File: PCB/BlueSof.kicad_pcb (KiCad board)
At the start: 2 copper layers, 134.3 x 100.2 mm, 117 parts, among them J1 USB_C_Receptacle_USB2.0, J2 Conn_01x01_Female, J3 Conn_01x04_Female, J4 Conn_01x01_Female, J5 USB_C_Receptacle_USB2.0, Q1 A03407, Q2 A03407, SW1 SW_PUSH, SW10 SW_PUSH, SW11 SW_PUSH, SW12 SW_PUSH, SW13 SW_PUSH, SW14 SW_PUSH, SW15 SW_PUSH, SW16 SW_PUSH, SW17 SW_PUSH, SW18 SW_PUSH, SW19 SW_PUSH, SW2 SW_PUSH, SW20 SW_PUSH, SW21 SW_PUSH, SW22 SW_PUSH, SW23 SW_PUSH, SW24 SW_PUSH, SW25 Rotary_Encoder_Switch, SW26 SW_PUSH, SW27 SW_PUSH, SW28 SW_PUSH, SW29 SW_PUSH, SW3 SW_PUSH, SW30 SW_PUSH, SW31 SW_Push, SW32 SW_Push, SW4 SW_PUSH, SW5 SW_PUSH, SW6 SW_PUSH, SW7 SW_PUSH, SW8 SW_PUSH, SW9 SW_PUSH, U1 LN2054Y42AMR, U2 E73-2G4M08S1C, U3 AP2112K-3.3, U4 E73-2G4M08S1C, U5 LN2054Y42AMR, U6 AP2112K-3.3, Y1 32.768kHz, Y2 32.768kHz

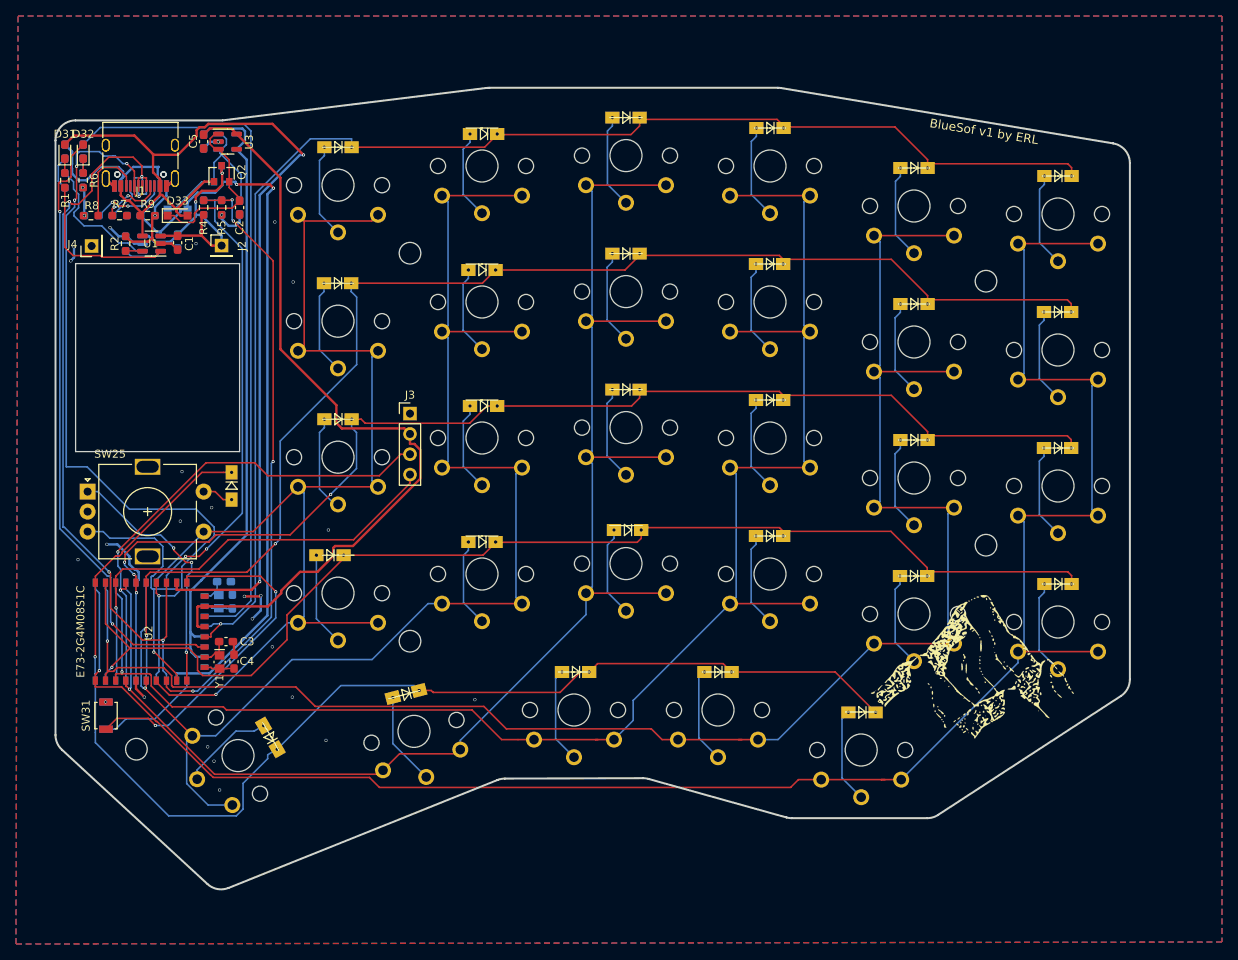
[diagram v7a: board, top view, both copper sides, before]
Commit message: R2 version with minor fixes
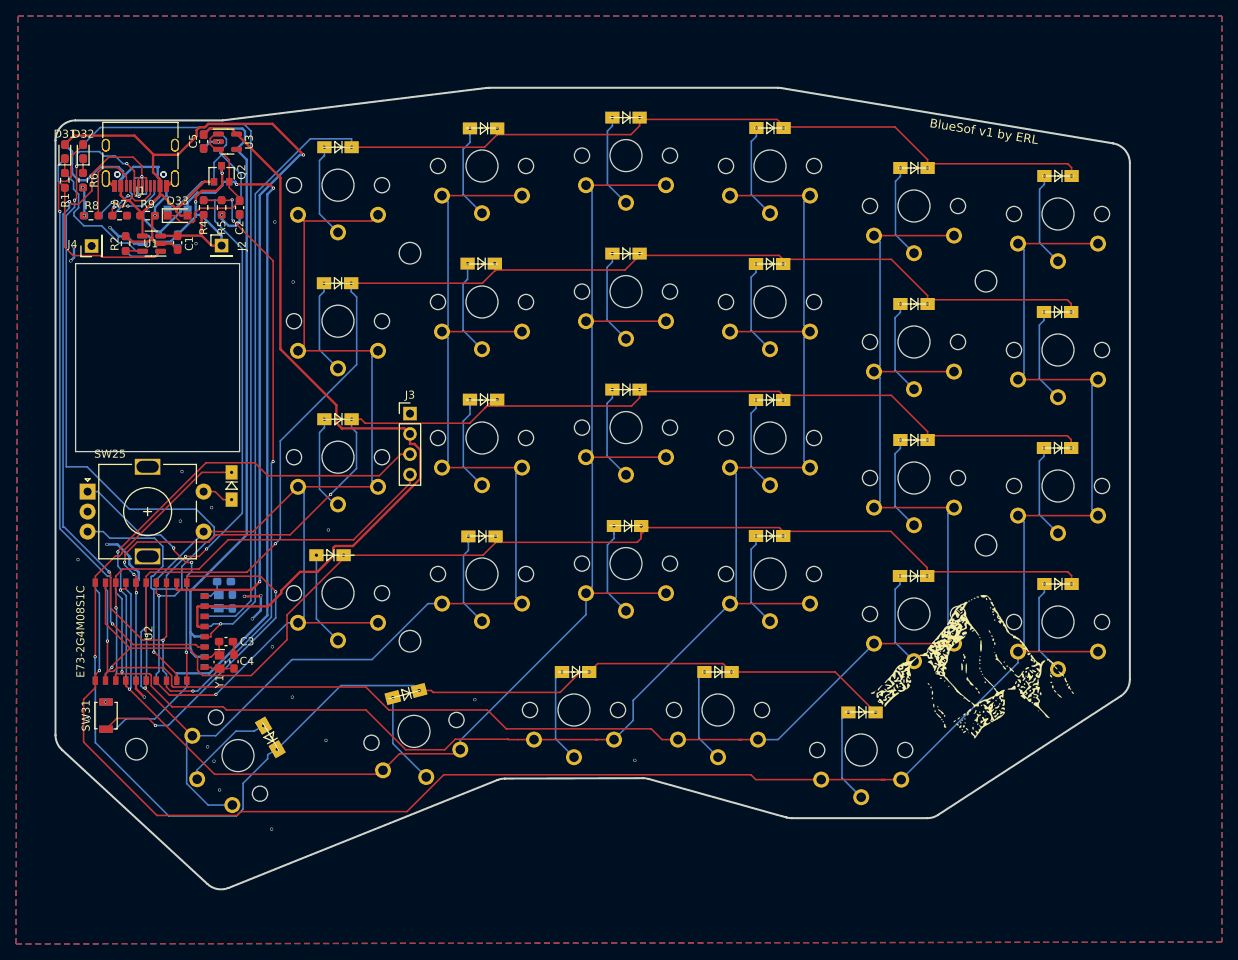
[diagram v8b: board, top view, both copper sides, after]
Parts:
- moved D8 0.81 mm to (139.4, 63.9)
- moved D14 0.80 mm to (139.7, 80.9)
- moved D2 0.70 mm to (139.7, 47.0)
- moved D20 0.70 mm to (139.5, 98.0)
- moved D21 0.50 mm to (157.7, 96.7)
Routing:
- net col0: track 235.2 -> 244.8 mm
- net row3: track 150.4 -> 152.5 mm
- net row2: track 153.7 -> 155.7 mm
- net Net-(D14-Pad2): track 11.2 -> 12.3 mm
- net col2: track 195.2 -> 196.3 mm
- net Net-(D21-Pad2): track 11.4 -> 12.4 mm
- net row1: track 164.6 -> 165.5 mm
- net Net-(D20-Pad2): track 11.1 -> 11.9 mm
- net Net-(D2-Pad2): track 11.2 -> 12.0 mm
- net row0: track 174.3 -> 175.0 mm
- net Net-(D8-Pad2): track 11.2 -> 11.9 mm
- net GND: vias 29 -> 32
